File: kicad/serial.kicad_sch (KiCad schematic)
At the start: 14 parts, among them J7 DSUB-9, J8 USB C, U25 MAX232, U26 CH340N

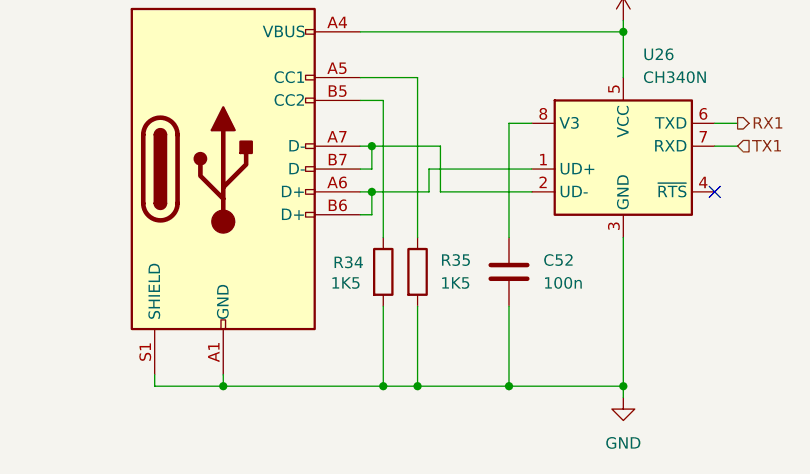
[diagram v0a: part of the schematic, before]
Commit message: Fix wrong D-SUB footprints, rev C
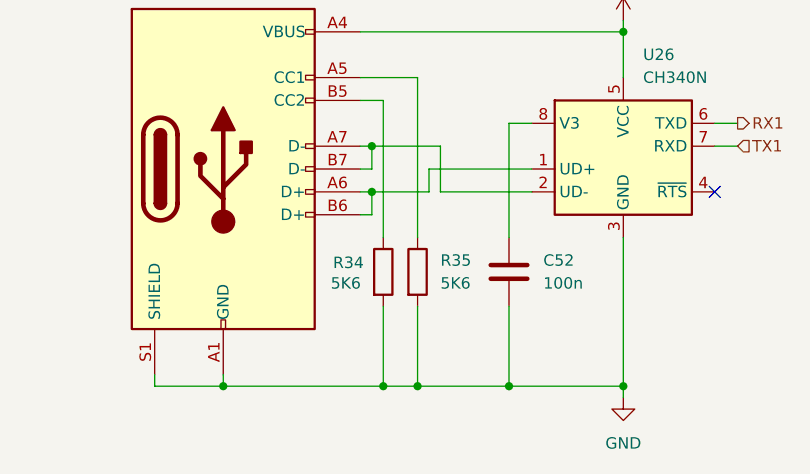
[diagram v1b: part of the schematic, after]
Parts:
- J7: footprint Connector_Dsub:DSUB-9_Socket_Horizontal_P2.77x2.84mm_EdgePinOffset4.94mm_Housed_MountingHolesOffset4.94mm -> Connector_Dsub:DSUB-9_Pins_Horizontal_P2.77x2.84mm_EdgePinOffset9.90mm_Housed_MountingHolesOffset11.32mm
- R34, R35: value 1K5 -> 5K6
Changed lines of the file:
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@@
 	(title_block
 		(title "UART")
-		(date "2025-07-03")
-		(rev "B")
+		(date "2025-07-20")
+		(rev "C")
 		(company "A.K.")
 	)
@@
 			)
 		)
-		(property "Value" "1K5"
+		(property "Value" "5K6"
 			(at 133.35 146.0499 0)
 			(effects
@@
 			)
 		)
-		(property "Footprint" "Connector_Dsub:DSUB-9_Socket_Horizontal_P2.77x2.84mm_EdgePinOffset4.94mm_Housed_MountingHolesOffset4.94mm"
+		(property "Footprint" "Connector_Dsub:DSUB-9_Pins_Horizontal_P2.77x2.84mm_EdgePinOffset9.90mm_Housed_MountingHolesOffset11.32mm"
 			(at 186.69 67.31 0)
 			(effects
@@
 			)
 		)
-		(property "Value" "1K5"
+		(property "Value" "5K6"
 			(at 121.158 146.05 0)
 			(effects

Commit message: rev D
- Fix SUB-D footprints yet again,
- rotate keyboard connector to remove cable twist,
- add onboard speaker.
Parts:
- J7: footprint Connector_Dsub:DSUB-9_Pins_Horizontal_P2.77x2.84mm_EdgePinOffset9.90mm_Housed_MountingHolesOffset11.32mm -> Connector_Dsub:DSUB-9_Pins_Horizontal_P2.77x2.84mm_EdgePinOffset7.70mm_Housed_MountingHolesOffset9.12mm
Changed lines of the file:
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@@
 	(title_block
 		(title "UART")
-		(date "2025-07-20")
-		(rev "C")
+		(date "2025-08-02")
+		(rev "D")
 		(company "A.K.")
 	)
@@
 			)
 		)
-		(property "Footprint" "Connector_Dsub:DSUB-9_Pins_Horizontal_P2.77x2.84mm_EdgePinOffset9.90mm_Housed_MountingHolesOffset11.32mm"
+		(property "Footprint" "Connector_Dsub:DSUB-9_Pins_Horizontal_P2.77x2.84mm_EdgePinOffset7.70mm_Housed_MountingHolesOffset9.12mm"
 			(at 186.69 67.31 0)
 			(effects

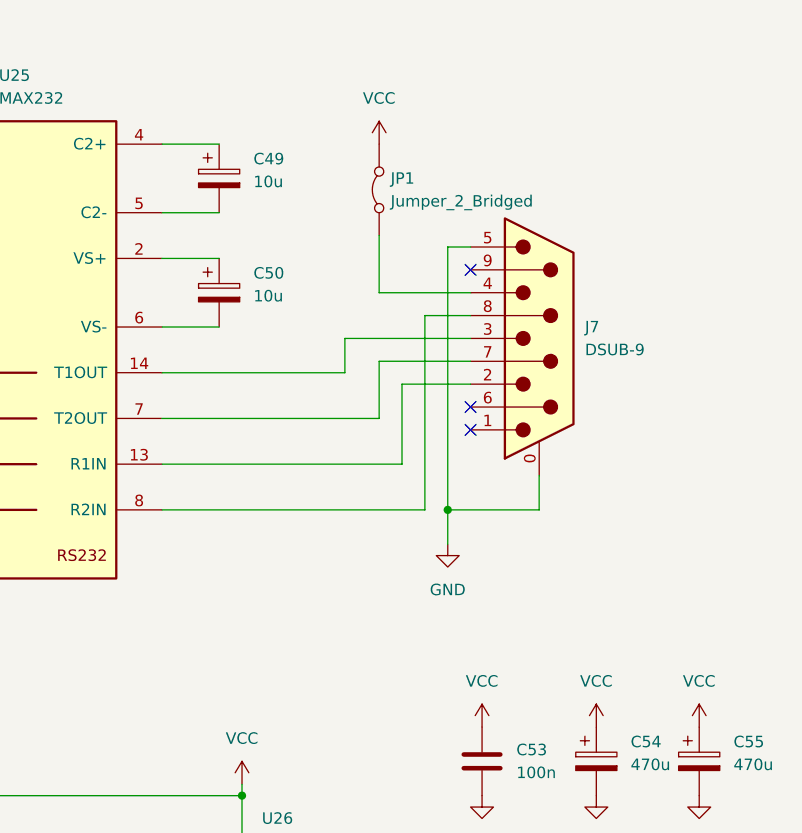
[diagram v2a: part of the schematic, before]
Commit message: Rev E: fix MAX232 usage
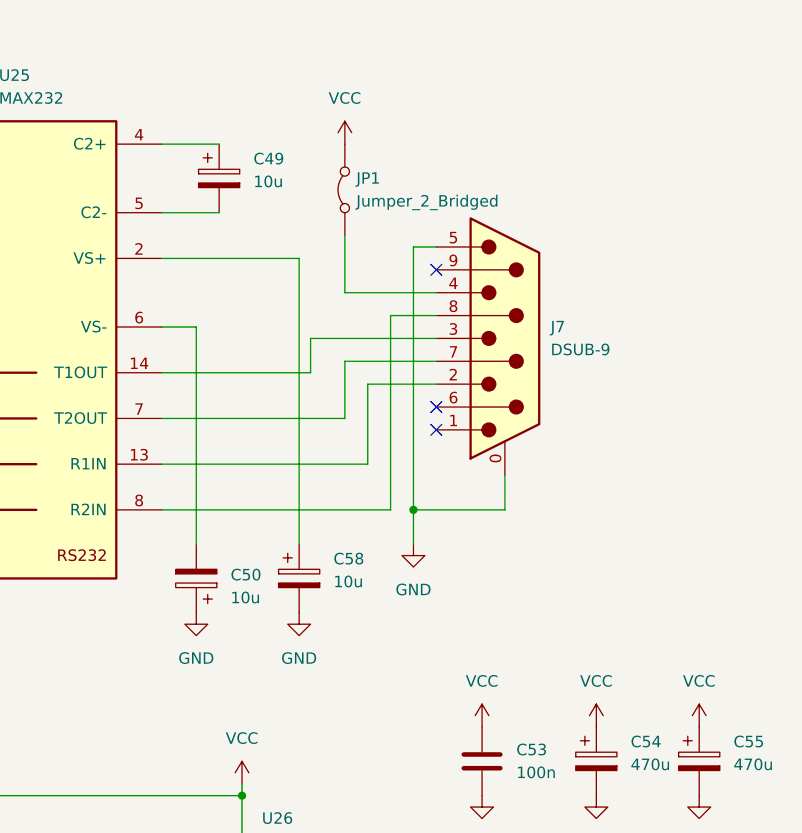
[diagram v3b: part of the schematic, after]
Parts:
- added C58: 10u, Capacitor_THT:CP_Radial_D5.0mm_P2.50mm, symbol Device:C_Polarized
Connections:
- net GND: now also C50.1, C58.2
- net at U25.2 (VS+): now also C58.1; no longer C50.1
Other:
- moved on the sheet: C50, J7, JP1
